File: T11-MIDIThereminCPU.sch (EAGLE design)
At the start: 55 parts, among them IC1 UA78M05DCY, IC5 4069D, J1 DCJ0202, Q1 16MHz, U1 ATMEGA328P-AU

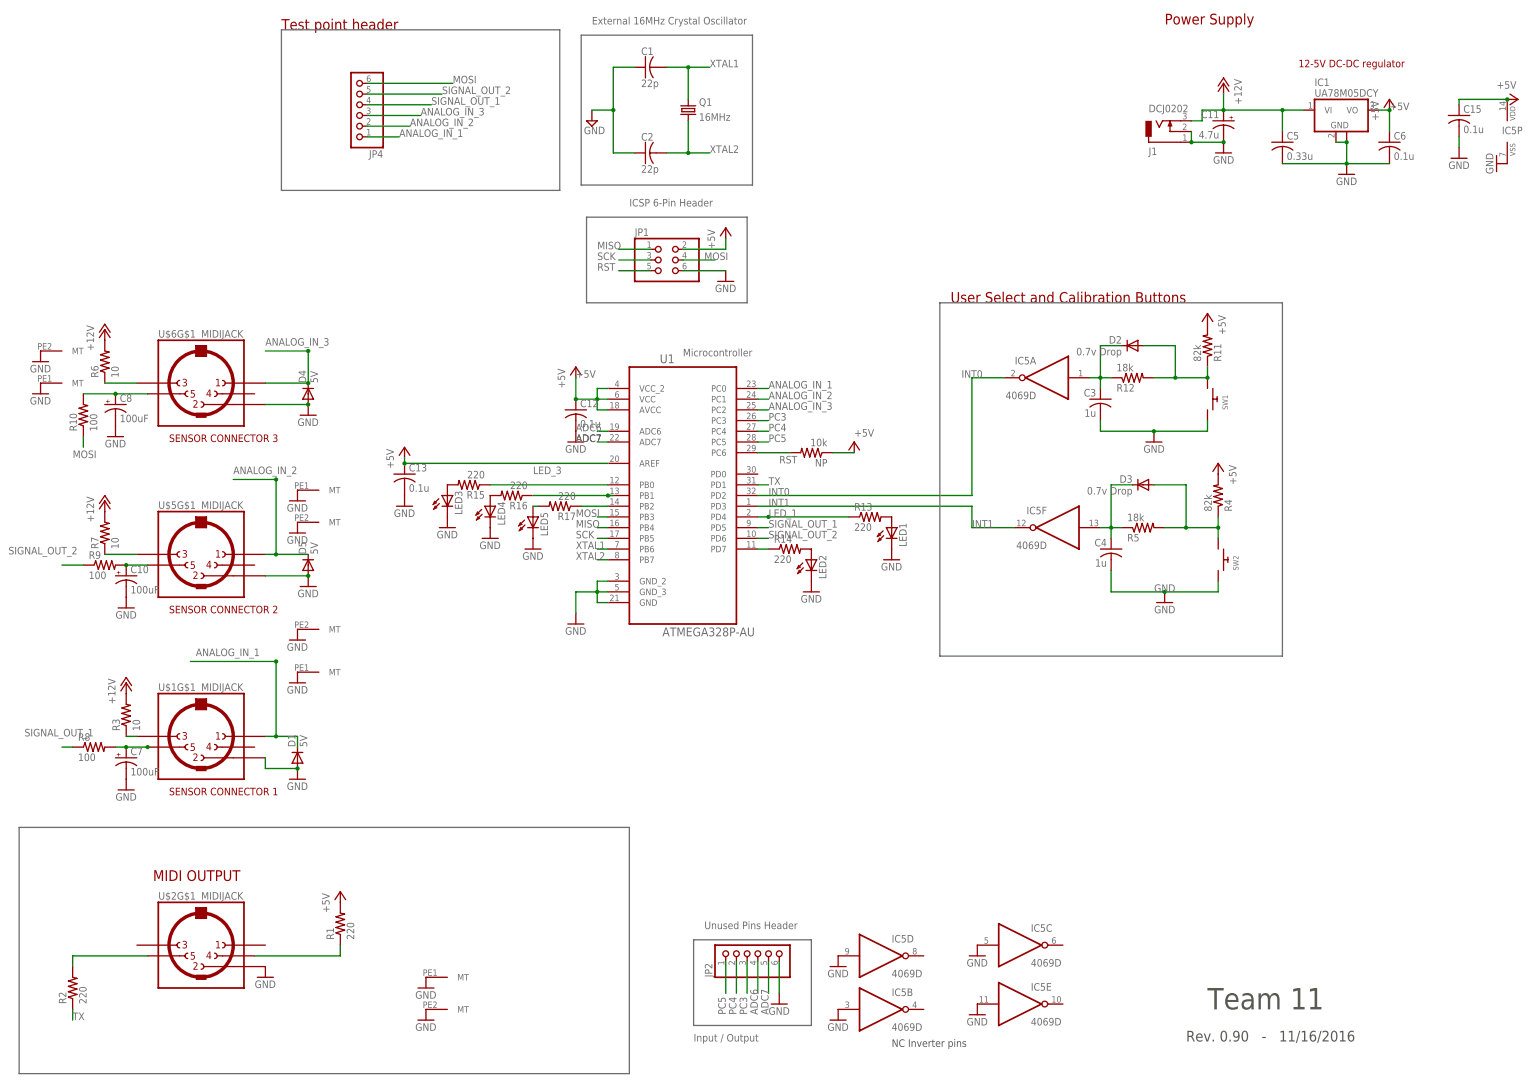
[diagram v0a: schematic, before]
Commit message: added a jumper to the MOSI line for programming
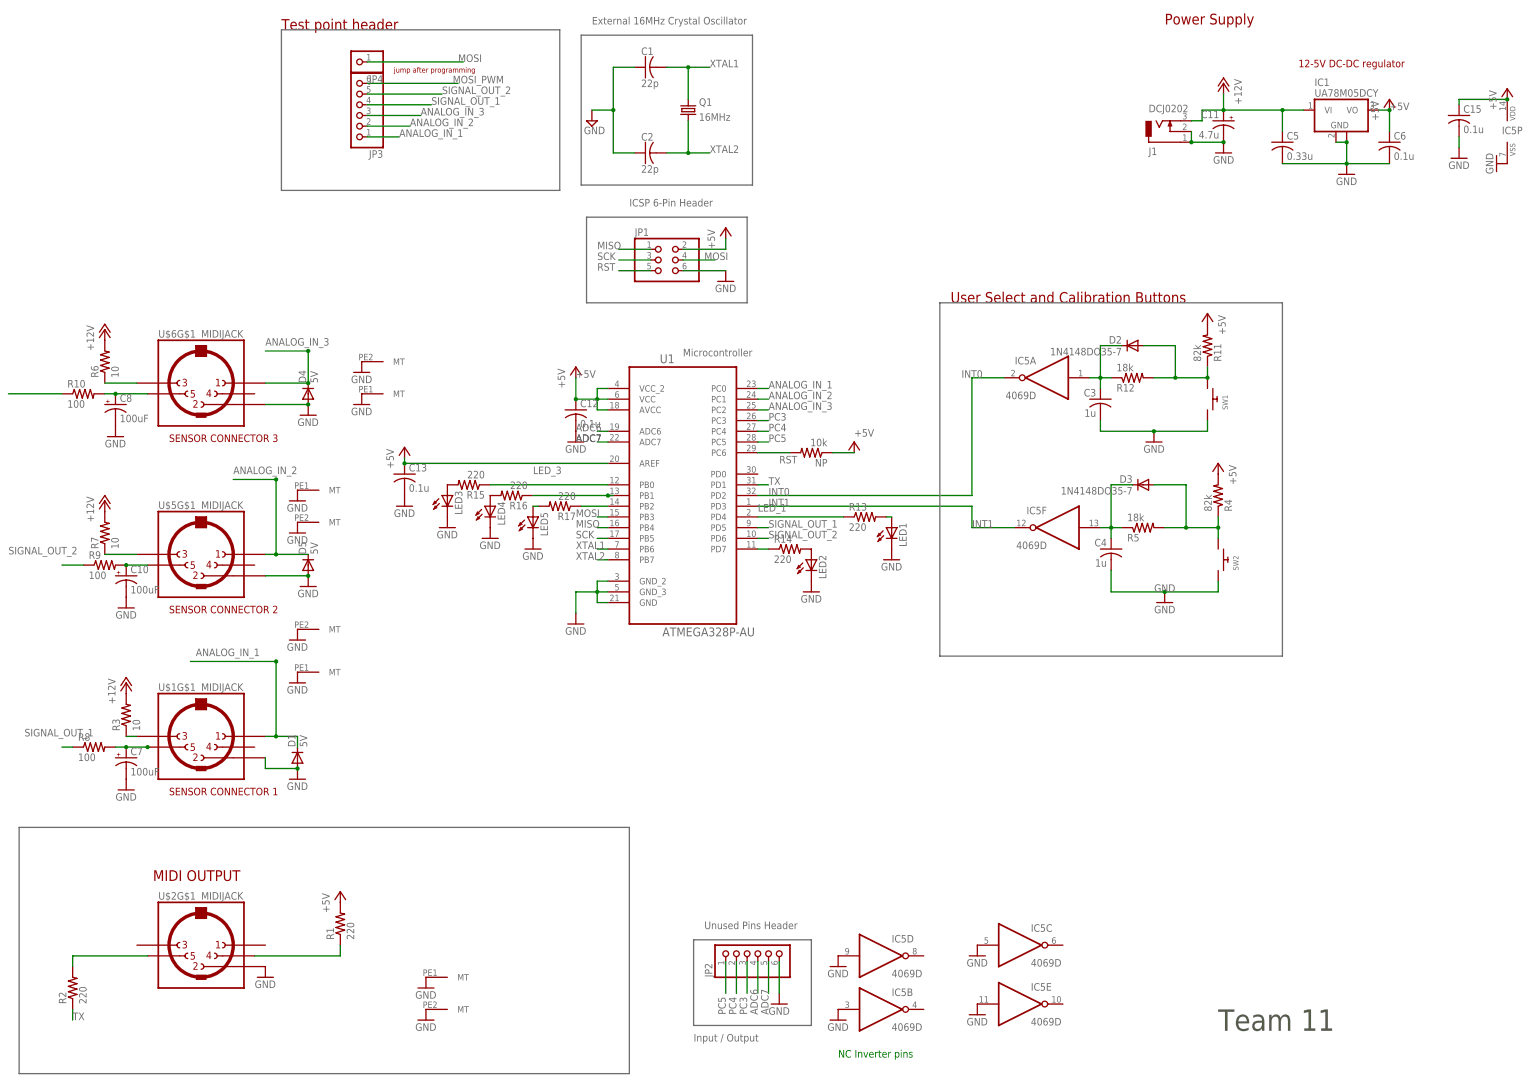
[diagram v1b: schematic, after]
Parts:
- added JP3: (no value), adafruit:PINHD-1X6
- D2, D3: value 0.7v Drop -> 1N4148DO35-7
- IC1: DIGIKEYNUMBER 296-12290-1-ND -> (none); PARTNUMBER UA78M05CDCYR -> (none)
- IC5: DIGIKEYNUMBER 296-28484-1-ND -> (none); PARTNUMBER SN7414DR -> (none)
- JP4: device adafruit:PINHD-1X6 -> adafruit:PINHD-1X1
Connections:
- new net MOSI_PWM: JP3.6, R10.1
- net ANALOG_IN_1: now also JP3.1; no longer JP4.1
- net ANALOG_IN_2: now also JP3.2; no longer JP4.2
- net ANALOG_IN_3: now also JP3.3; no longer JP4.3
- net MOSI: now also JP4.1; no longer JP4.6, R10.1
- net SIGNAL_OUT_1: now also JP3.4; no longer JP4.4
- net SIGNAL_OUT_2: now also JP3.5; no longer JP4.5
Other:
- note added: "jump after programming"
- note removed: "Rev. 0.90 - 11/16/2016"
- moved on the sheet: R10, R13

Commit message: removed debounce circuit. added vias
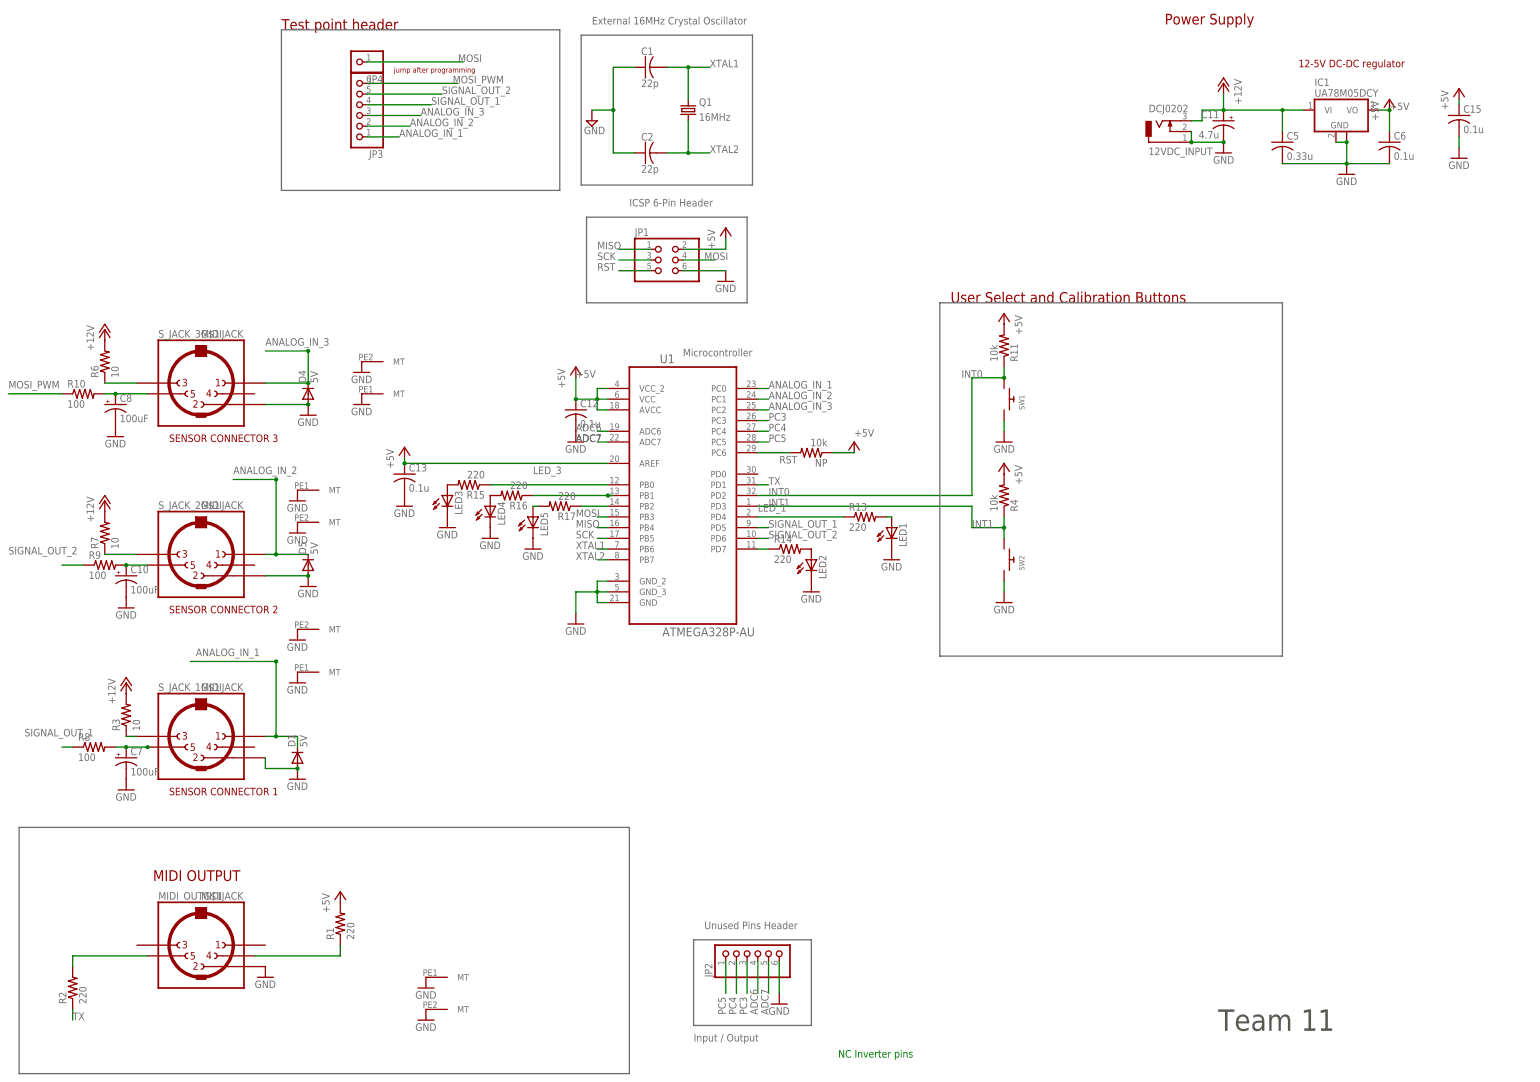
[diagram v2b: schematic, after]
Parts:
- removed C3, C4: 1u, adafruit:C-USC0805
- removed D2, D3: 1N4148DO35-7, diode:1N4148DO35-7
- removed IC5: 4069D, 40xx:4069D
- removed R12, R5: 18k, resistor:R-US_R0805
- R11, R4: value 82k -> 10k
- renumbered J1 to 12VDC_INPUT, U$1 to S_JACK_1, U$2 to MIDI_OUT, U$5 to S_JACK_2, U$6 to S_JACK_3
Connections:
- removed net N$11: D2.A, R11.1, R12.2, SW1.P$2
- removed net N$14: C3.1, D2.C, IC5A.I, R12.1
- removed net N$4: D3.A, R4.1, R5.2, SW2.P$2
- removed net N$6: C4.1, D3.C, IC5F.I, R5.1
- net +5V: no longer IC5P.VDD
- net GND: no longer C3.2, C4.2, IC5B.I, IC5C.I, IC5D.I, IC5E.I, IC5P.VSS
- net INT0: now also R11.1, SW1.P$2; no longer IC5A.O
- net INT1: now also R4.1, SW2.P$2; no longer IC5F.O
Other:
- moved on the sheet: R11, R4, SW1, SW2

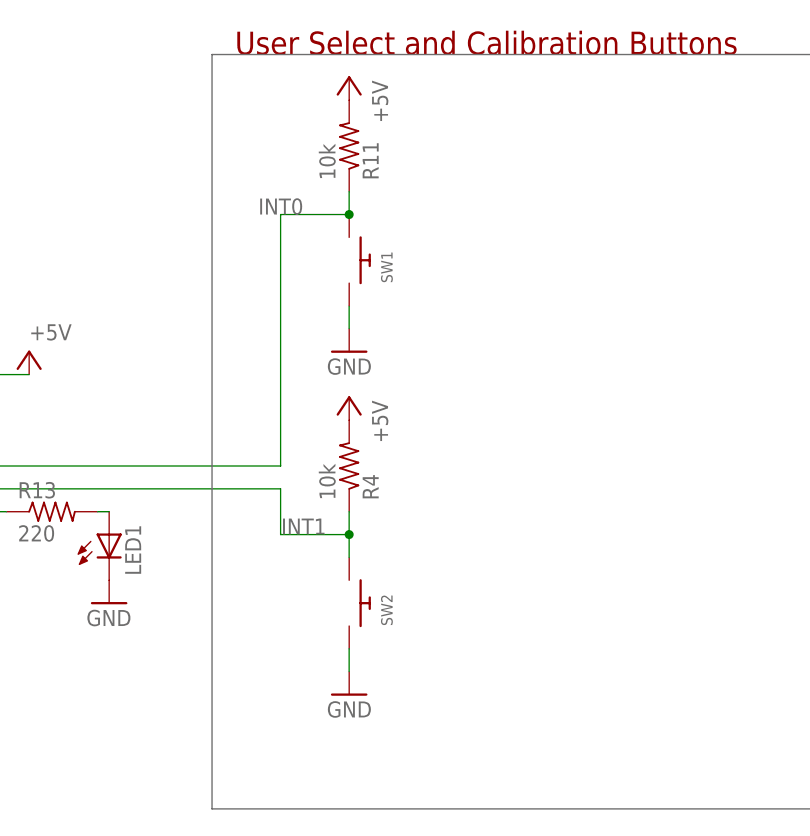
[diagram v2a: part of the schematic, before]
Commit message: added optional panel mount buttons
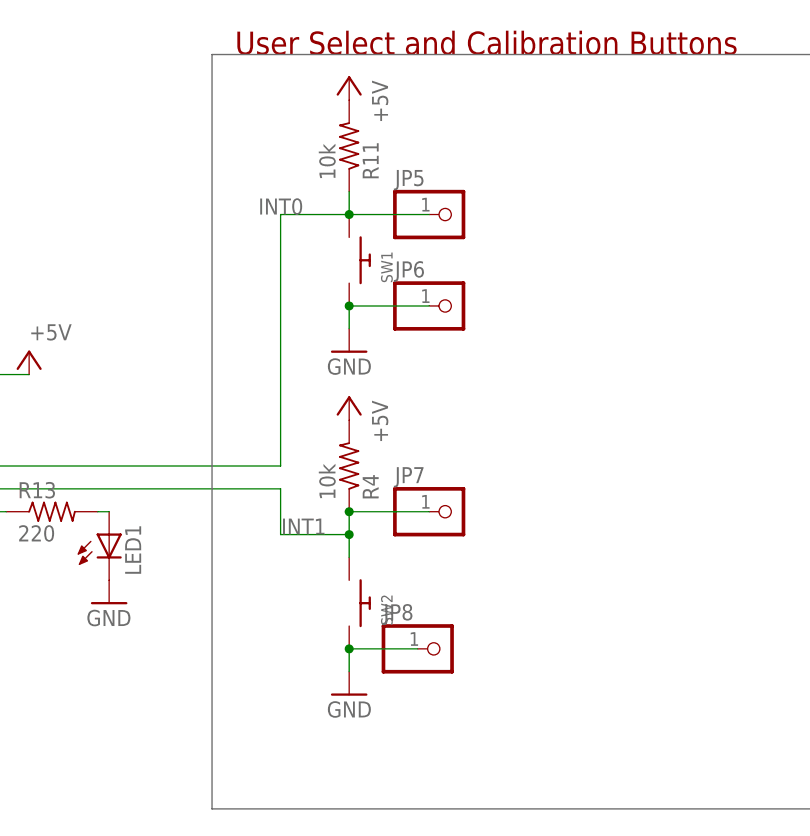
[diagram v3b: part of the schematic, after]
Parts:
- added JP5, JP6, JP7, JP8: (no value), pinhead:PINHD-1X1
- JP4: device adafruit:PINHD-1X1 -> pinhead:PINHD-1X1
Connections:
- net GND: now also JP6.1, JP8.1
- net INT0: now also JP5.1
- net INT1: now also JP7.1
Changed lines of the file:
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@@
 <part name="GND28" library="supply1" deviceset="GND" device=""/>
 <part name="GND29" library="supply1" deviceset="GND" device=""/>
-<part name="JP4" library="adafruit" deviceset="PINHD-1X1" device=""/>
+<part name="JP4" library="pinhead" deviceset="PINHD-1X1" device=""/>
 <part name="JP3" library="adafruit" deviceset="PINHD-1X6" device=""/>
+<part name="JP5" library="pinhead" deviceset="PINHD-1X1" device=""/>
+<part name="JP6" library="pinhead" deviceset="PINHD-1X1" device=""/>
+<part name="JP7" library="pinhead" deviceset="PINHD-1X1" device=""/>
+<part name="JP8" library="pinhead" deviceset="PINHD-1X1" device=""/>
 </parts>
 <sheets>
@@
 <instance part="JP4" gate="G$1" x="100.33" y="240.03" rot="R180"/>
 <instance part="JP3" gate="A" x="100.33" y="229.87" rot="R180"/>
+<instance part="JP5" gate="G$1" x="265.43" y="165.1"/>
+<instance part="JP6" gate="G$1" x="265.43" y="154.94"/>
+<instance part="JP7" gate="G$1" x="265.43" y="132.08"/>
+<instance part="JP8" gate="G$1" x="264.16" y="116.84"/>
 </instances>
 <busses>
@@
 <wire x1="254" y1="154.94" x2="254" y2="152.4" width="0.1524" layer="91"/>
 <pinref part="GND4" gate="1" pin="GND"/>
+<pinref part="JP6" gate="G$1" pin="1"/>
+<wire x1="262.89" y1="154.94" x2="254" y2="154.94" width="0.1524" layer="91"/>
+<junction x="254" y="154.94"/>
 </segment>
 <segment>
@@
 <wire x1="254" y1="116.84" x2="254" y2="114.3" width="0.1524" layer="91"/>
 <pinref part="GND3" gate="1" pin="GND"/>
+<pinref part="JP8" gate="G$1" pin="1"/>
+<wire x1="261.62" y1="116.84" x2="254" y2="116.84" width="0.1524" layer="91"/>
+<junction x="254" y="116.84"/>
 </segment>
 <segment>
@@
 <wire x1="246.38" y1="165.1" x2="254" y2="165.1" width="0.1524" layer="91"/>
 <junction x="254" y="165.1"/>
+<pinref part="JP5" gate="G$1" pin="1"/>
+<wire x1="262.89" y1="165.1" x2="254" y2="165.1" width="0.1524" layer="91"/>
 </segment>
 </net>
@@
 <wire x1="246.38" y1="129.54" x2="254" y2="129.54" width="0.1524" layer="91"/>
 <junction x="254" y="129.54"/>
-</segment>
-</net>
+<pinref part="JP7" gate="G$1" pin="1"/>
+<wire x1="262.89" y1="132.08" x2="254" y2="132.08" width="0.1524" layer="91"/>
+<junction x="254" y="132.08"/>
+</segment>
+</net>
